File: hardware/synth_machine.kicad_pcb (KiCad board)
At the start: 2 copper layers, 234.9 x 161.9 mm, 87 parts, among them J1 USB-C (MIDI + 5V power), J10 Pot Wave (10k lin, panel moun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, J11 Pot Attack (10k lin, panel mo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, J12 Pot Decay (10k lin, panel mou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, J13 Pot Sustain (10k lin, panel m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, J14 Pot Release (10k lin, panel m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, J4 From amp screw terminals (L+ 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, J5 Speaker L (JST-PH), J6 Speaker R (JST-PH), J7 Headphones 3.5mm (CUI SJ1-351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, J8 Expansion, Q1 2N3904, SW1 KEY C4 (direct D10) - 2x Keys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, SW10 D#4 [c4 r1] - 2x Keystone 3534, SW11 F#4 [c3 r1] - 2x Keystone 3534, SW12 G#4 [c2 r1] - 2x Keystone 3534, SW13 A#4 [c1 r1] - 2x Keystone 3534, SW14 BTN1 [c0 r0] - 2x Keystone 35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, SW15 BTN2 [c0 r1] - 2x Keystone 35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, SW16 BTN3 [c1 r0] - 2x Keystone 35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, SW17 BTN4 [c2 r0] - 2x Keystone 35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, SW18 BTN5 [c3 r0] - 2x Keystone 35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, SW19 BTN6 [c4 r0] - 2x Keystone 35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, SW2 D4 [c5 r1] - 2x Keystone 3534, SW3 E4 [c5 r2] - 2x Keystone 3534, SW4 F4 [c4 r2] - 2x Keystone 3534, SW5 G4 [c3 r2] - 2x Keystone 3534, SW6 A4 [c2 r2] - 2x Keystone 3534, SW7 B4 [c1 r2] - 2x Keystone 3534, SW8 C5 [c0 r2] - 2x Keystone 3534, SW9 C#4 [c5 r0] - 2x Keystone 3534, U1 Daisy Seed, U2 TPA6138A2PWR

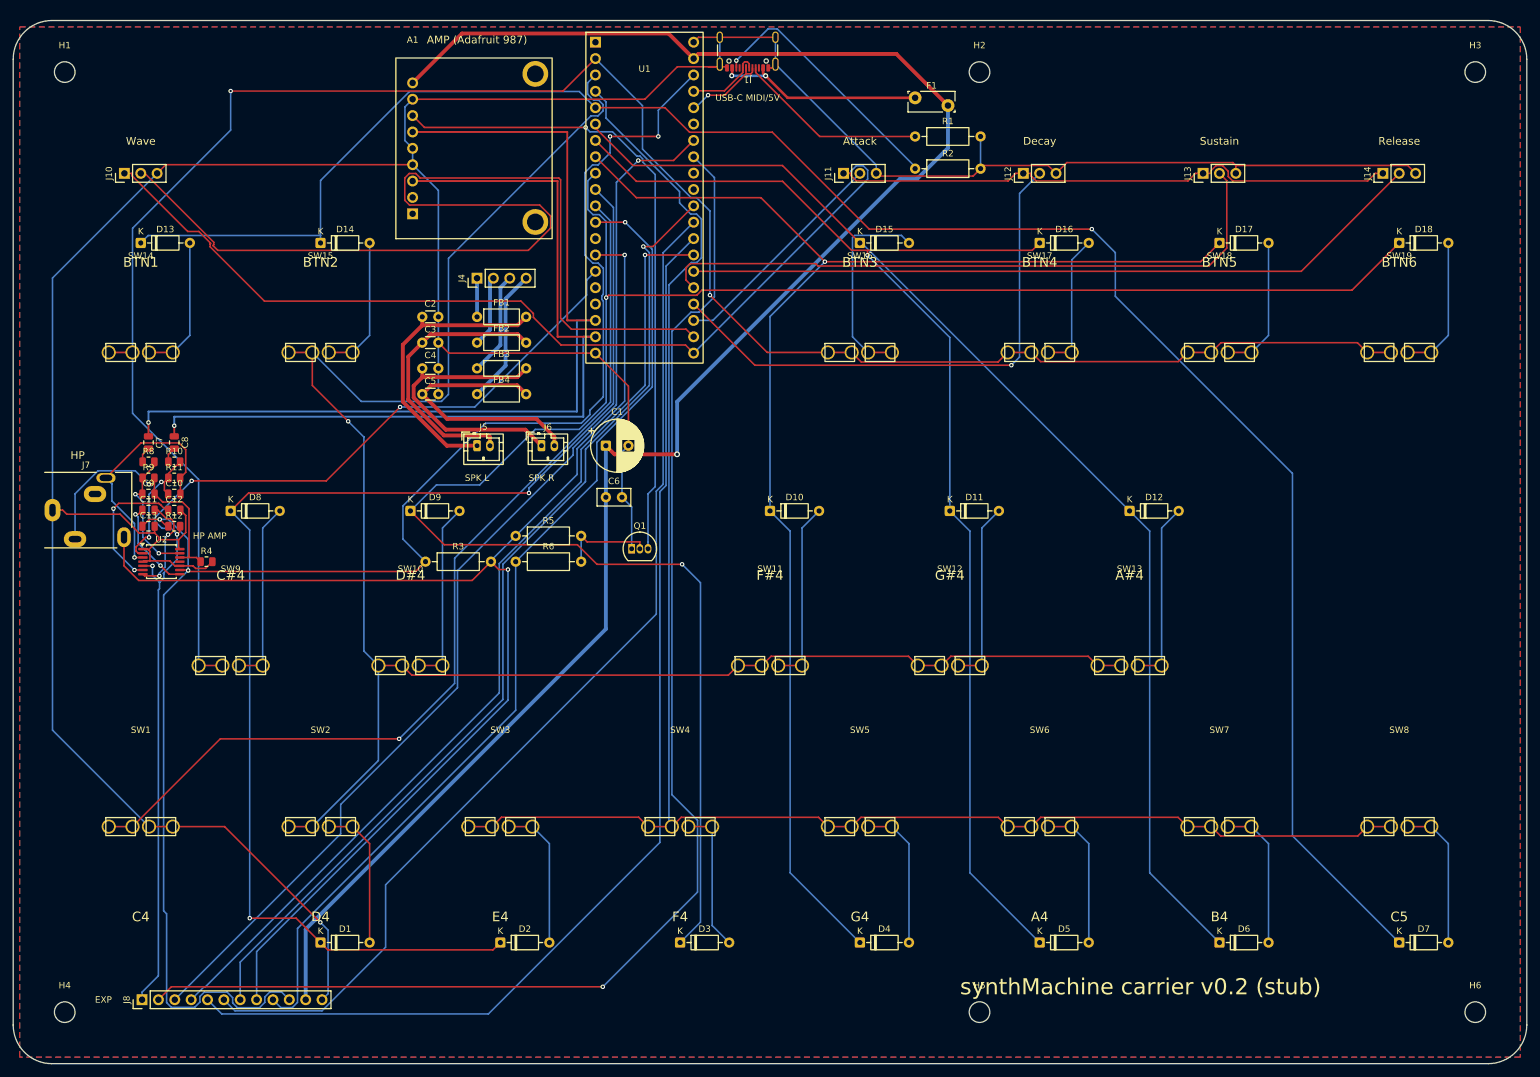
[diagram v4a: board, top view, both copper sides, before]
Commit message: Put the MAX98306 on the board and prepare for JLCPCB SMT assembly
- U3 MAX98306ETD+T (TDFN-14, thermal vias) replaces the Adafruit breakout
  header A1 and the speaker return header J4; 1u input caps, 10u + 100n
  decoupling, 100k SHDN pull-up, 100k gain resistor (9 dB) and a 3-pad
  solder jumper for 12/18 dB
- amp fan-out hand-routed: 0.2 mm stubs from the 0.4 mm pitch pads, vias,
  0.3 mm B.Cu bus to the ferrite beads; speaker nets renamed to P/N so
  KiCad/Freerouting stop treating them as differential pairs
- design rules 0.2 mm track / 0.15 mm clearance / 0.2 mm min drill
- all SMD passives are 0805 with LCSC codes; CC pull-downs and the
  headphone-detect resistors moved from axial to 0805
- fab.sh emits jlcpcb_bom.csv / jlcpcb_cpl.csv for top-side assembly
- routed: 915 segments, 61 vias, 0 unrouted, DRC clean apart from known nits

Co-Authored-By: Claude Fable 5.1 <noreply@anthropic.com>
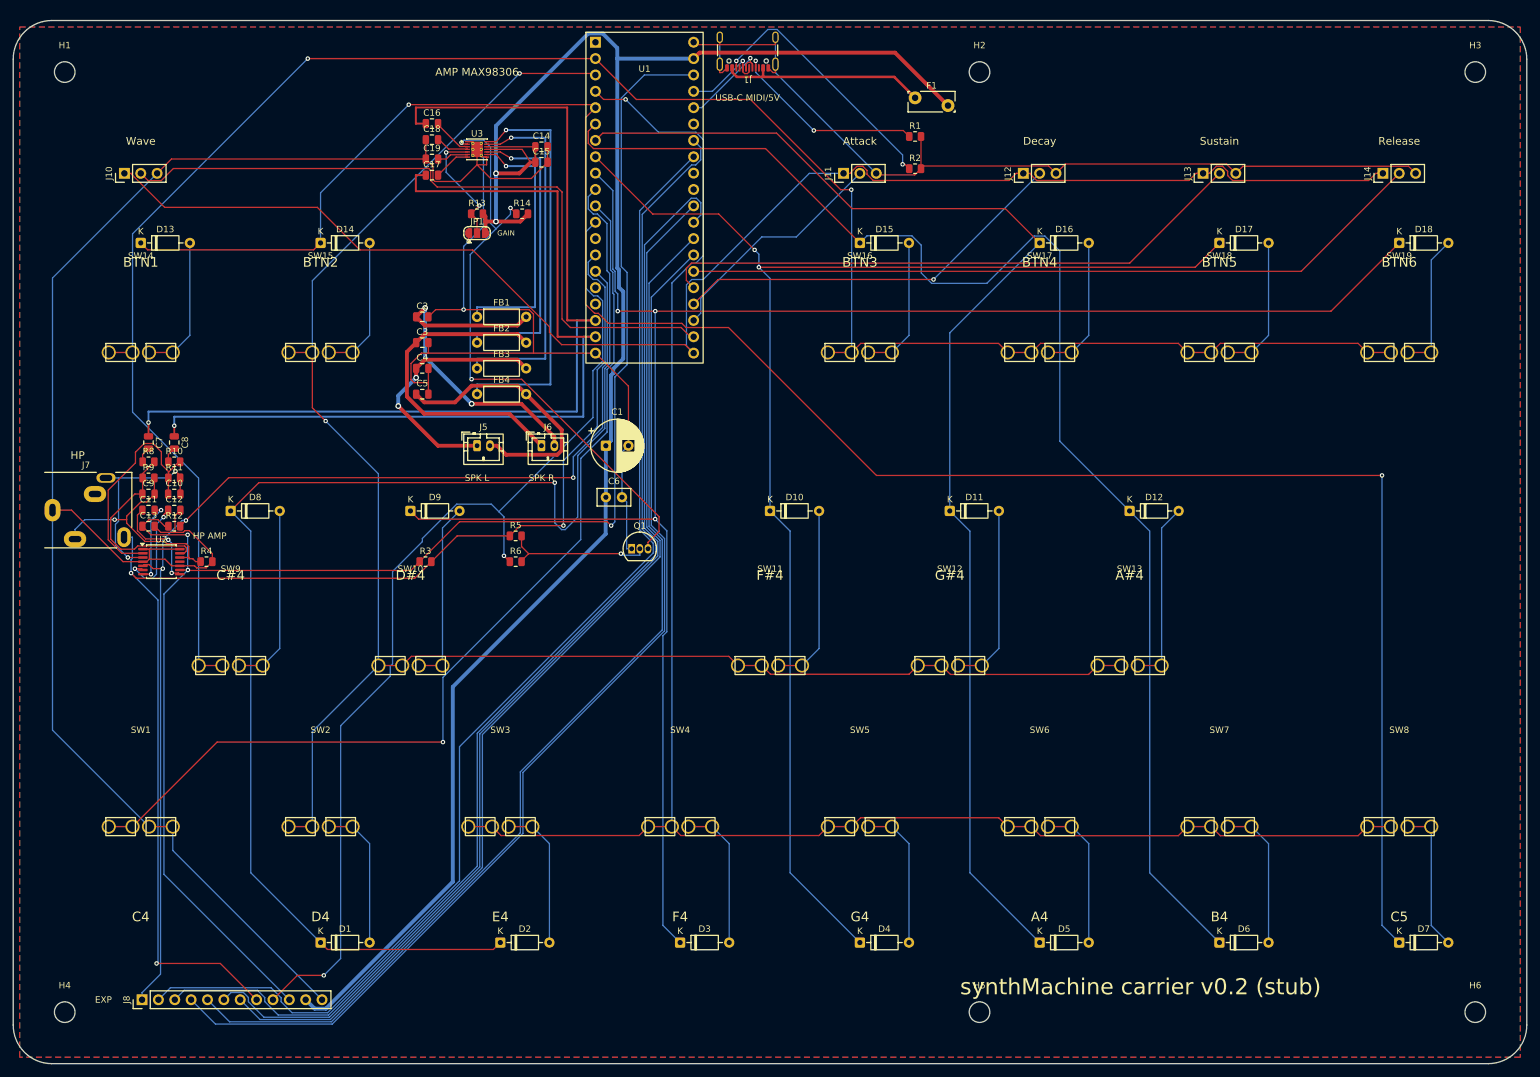
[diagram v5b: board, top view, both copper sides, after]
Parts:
- removed A1: Adafruit MAX98306 amp breakout, Adafruit_MAX98306_Breakout
- removed J4: From amp screw terminals (L+ L- R+ R-), PinHeader_1x04_P2.54mm_Vertical
- added C14: 10u, C_0805_2012Metric, F.Cu at (82.0, 19.6)
- added C15: 100n, C_0805_2012Metric, F.Cu at (82.0, 22.0)
- added C16: 1u, C_0805_2012Metric, F.Cu at (65.0, 16.0)
- added C17: 1u, C_0805_2012Metric, F.Cu at (65.0, 24.0)
- added C18: 1u, C_0805_2012Metric, F.Cu at (65.0, 18.5)
- added C19: 1u, C_0805_2012Metric, F.Cu at (65.0, 21.5)
- added JP1: GAIN: 1-2 = 18dB, open = R13, 2-3 = 12dB, SolderJumper-3_P1.3mm_Open_RoundedPad1.0x1.5mm, F.Cu at (72.0, 33.0)
- added R13: 100k, R_0805_2012Metric, F.Cu at (72.0, 30.0)
- added R14: 100k, R_0805_2012Metric, F.Cu at (79.0, 30.0)
- added U3: MAX98306ETD+T, TDFN-14-1EP_3x3mm_P0.4mm_EP1.78x2.35mm_ThermalVias, F.Cu at (72.0, 20.0)
- C13: value 2u2 -> 10u
- C2, C3, C4, C5: footprint C_Disc_D3.0mm_W1.6mm_P2.50mm -> C_0805_2012Metric
- R1, R2, R3, R5, R6: footprint R_Axial_DIN0207_L6.3mm_D2.5mm_P10.16mm_Horizontal -> R_0805_2012Metric
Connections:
- C2 pad 1: SPKF_L+ -> SPKF_RN
- C3 pad 1: SPKF_L- -> SPKF_RP
- C4 pad 1: SPKF_R+ -> SPKF_LP
- C5 pad 1: SPKF_R- -> SPKF_LN
- FB1 pad 1: SPK_L+ -> SPK_RN
- FB1 pad 2: SPKF_L+ -> SPKF_RN
- FB2 pad 1: SPK_L- -> SPK_RP
- FB2 pad 2: SPKF_L- -> SPKF_RP
- FB3 pad 1: SPK_R+ -> SPK_LP
- FB3 pad 2: SPKF_R+ -> SPKF_LP
- FB4 pad 1: SPK_R- -> SPK_LN
- FB4 pad 2: SPKF_R- -> SPKF_LN
- J5 pad 1: SPKF_L+ -> SPKF_LP
- J5 pad 2: SPKF_L- -> SPKF_LN
- J6 pad 1: SPKF_R+ -> SPKF_RP
- J6 pad 2: SPKF_R- -> SPKF_RN
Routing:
- net SPK_LN: track 0.00 -> 63.2 mm, vias 0 -> 1
- net POT_WAVE: track 167.7 -> 110.4 mm
- net SPK_LP: track 0.00 -> 55.8 mm, vias 0 -> 1
- net SPKF_RN: track 0.00 -> 54.4 mm, vias 0 -> 2
- net SPKF_RP: track 0.00 -> 51.2 mm
- net SPK_RP: track 0.00 -> 47.0 mm, vias 0 -> 1
- net SPKF_L+: track 45.4 -> 0.00 mm
- net SPKF_R+: track 44.7 -> 0.00 mm
- net SPKF_L-: track 43.4 -> 0.00 mm
- net SPKF_LN: track 0.00 -> 42.2 mm
- net SPKF_R-: track 41.9 -> 0.00 mm
- net SPK_RN: track 0.00 -> 40.8 mm, vias 0 -> 1
- net SPKF_LP: track 0.00 -> 40.0 mm, vias 0 -> 2
- net COL1: track 180.9 -> 210.7 mm
- net EXP_D26: track 211.2 -> 187.2 mm, vias 1 -> 0
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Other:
- board text added: "AMP MAX98306"
- board text added: "GAIN"
- board text removed: "AMP (Adafruit 987)"

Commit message: Carrier v0.3: compact 100x100 board, JST-XH leads for buttons and pots
- Buttons no longer plug into the board: one JST-XH 2-pin header per key
  (10 down the left edge, 9 along the bottom), pots on JST-XH 3-pin headers
  down the right edge; board shrinks to 100 x 100 mm (JLC cheap tier)
- USB-C, headphone jack and the Seed's own USB all on the top edge
- Seed3 supported (same pinout/outline as the original Seed)
- more SMT for JLC: 1N4148W SOD-123 diodes, 0805 ferrite beads, MMBT3904
  SOT-23, 0805 100n; hand-solder list is now connectors, sockets, fuse, C1
- audio pre-routes reworked for the new geometry (no crossings), amp
  fan-out kept; 808 segments, 46 vias, 0 unrouted, DRC clean apart from the
  known library nits
- README rewritten; Digi-Key list rewritten for the XH connectors

Co-Authored-By: Claude Fable 5.1 <noreply@anthropic.com>
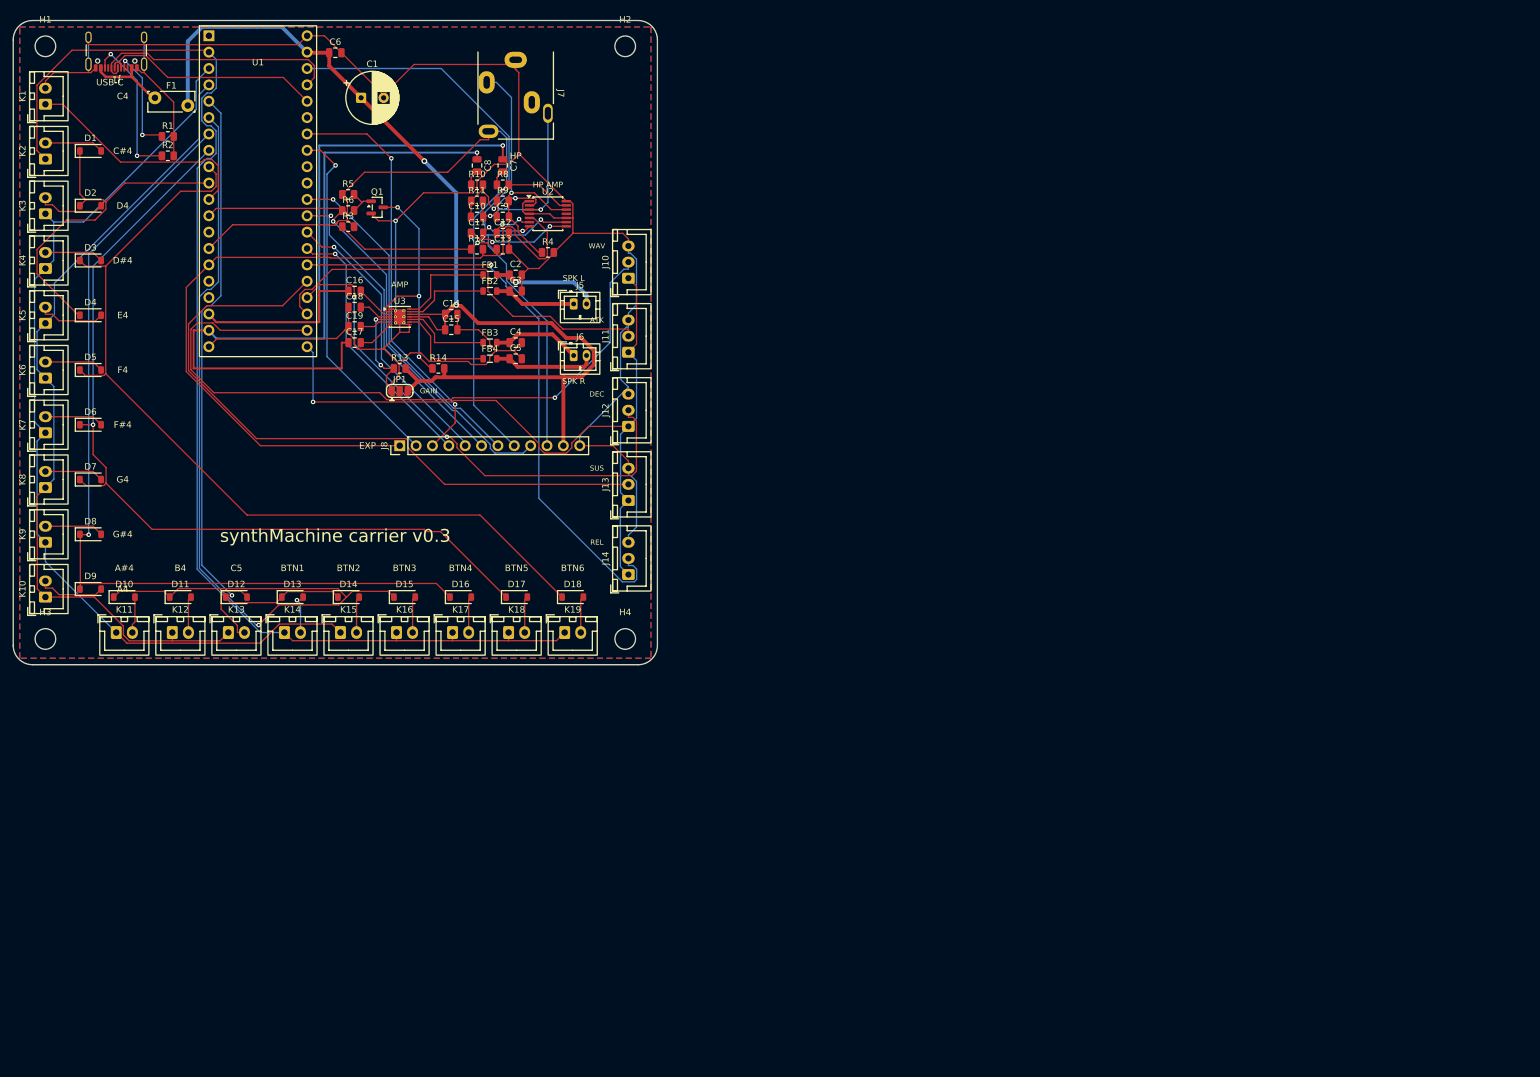
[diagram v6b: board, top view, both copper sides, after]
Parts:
- removed H5, H6: M3, MountingHole_3.2mm_M3
- removed SW1: KEY C4 (direct D10) - 2x Keystone 3534, ArcadeButton_24mm_Keystone3534
- removed SW10: D#4 [c4 r1] - 2x Keystone 3534, ArcadeButton_24mm_Keystone3534
- removed SW11: F#4 [c3 r1] - 2x Keystone 3534, ArcadeButton_24mm_Keystone3534
- removed SW12: G#4 [c2 r1] - 2x Keystone 3534, ArcadeButton_24mm_Keystone3534
- removed SW13: A#4 [c1 r1] - 2x Keystone 3534, ArcadeButton_24mm_Keystone3534
- removed SW14: BTN1 [c0 r0] - 2x Keystone 3534, ArcadeButton_24mm_Keystone3534
- removed SW15: BTN2 [c0 r1] - 2x Keystone 3534, ArcadeButton_24mm_Keystone3534
- removed SW16: BTN3 [c1 r0] - 2x Keystone 3534, ArcadeButton_24mm_Keystone3534
- removed SW17: BTN4 [c2 r0] - 2x Keystone 3534, ArcadeButton_24mm_Keystone3534
- removed SW18: BTN5 [c3 r0] - 2x Keystone 3534, ArcadeButton_24mm_Keystone3534
- removed SW19: BTN6 [c4 r0] - 2x Keystone 3534, ArcadeButton_24mm_Keystone3534
- removed SW2: D4 [c5 r1] - 2x Keystone 3534, ArcadeButton_24mm_Keystone3534
- removed SW3: E4 [c5 r2] - 2x Keystone 3534, ArcadeButton_24mm_Keystone3534
- removed SW4: F4 [c4 r2] - 2x Keystone 3534, ArcadeButton_24mm_Keystone3534
- removed SW5: G4 [c3 r2] - 2x Keystone 3534, ArcadeButton_24mm_Keystone3534
- removed SW6: A4 [c2 r2] - 2x Keystone 3534, ArcadeButton_24mm_Keystone3534
- removed SW7: B4 [c1 r2] - 2x Keystone 3534, ArcadeButton_24mm_Keystone3534
- removed SW8: C5 [c0 r2] - 2x Keystone 3534, ArcadeButton_24mm_Keystone3534
- removed SW9: C#4 [c5 r0] - 2x Keystone 3534, ArcadeButton_24mm_Keystone3534
- added K1: KEY C4 (direct D10) JST-XH, JST_XH_B2B-XH-A_1x02_P2.50mm_Vertical, F.Cu at (5.00, 13.0)
- added K10: A4 [c2 r2] JST-XH, JST_XH_B2B-XH-A_1x02_P2.50mm_Vertical, F.Cu at (5.00, 89.5)
- added K11: A#4 [c1 r1] JST-XH, JST_XH_B2B-XH-A_1x02_P2.50mm_Vertical, F.Cu at (16.0, 95.0)
- added K12: B4 [c1 r2] JST-XH, JST_XH_B2B-XH-A_1x02_P2.50mm_Vertical, F.Cu at (24.7, 95.0)
- added K13: C5 [c0 r2] JST-XH, JST_XH_B2B-XH-A_1x02_P2.50mm_Vertical, F.Cu at (33.4, 95.0)
- added K14: BTN1 [c0 r0] JST-XH, JST_XH_B2B-XH-A_1x02_P2.50mm_Vertical, F.Cu at (42.1, 95.0)
- added K15: BTN2 [c0 r1] JST-XH, JST_XH_B2B-XH-A_1x02_P2.50mm_Vertical, F.Cu at (50.8, 95.0)
- added K16: BTN3 [c1 r0] JST-XH, JST_XH_B2B-XH-A_1x02_P2.50mm_Vertical, F.Cu at (59.5, 95.0)
- added K17: BTN4 [c2 r0] JST-XH, JST_XH_B2B-XH-A_1x02_P2.50mm_Vertical, F.Cu at (68.2, 95.0)
- added K18: BTN5 [c3 r0] JST-XH, JST_XH_B2B-XH-A_1x02_P2.50mm_Vertical, F.Cu at (76.9, 95.0)
- added K19: BTN6 [c4 r0] JST-XH, JST_XH_B2B-XH-A_1x02_P2.50mm_Vertical, F.Cu at (85.6, 95.0)
- added K2: C#4 [c5 r0] JST-XH, JST_XH_B2B-XH-A_1x02_P2.50mm_Vertical, F.Cu at (5.00, 21.5)
- added K3: D4 [c5 r1] JST-XH, JST_XH_B2B-XH-A_1x02_P2.50mm_Vertical, F.Cu at (5.00, 30.0)
- added K4: D#4 [c4 r1] JST-XH, JST_XH_B2B-XH-A_1x02_P2.50mm_Vertical, F.Cu at (5.00, 38.5)
- added K5: E4 [c5 r2] JST-XH, JST_XH_B2B-XH-A_1x02_P2.50mm_Vertical, F.Cu at (5.00, 47.0)
- added K6: F4 [c4 r2] JST-XH, JST_XH_B2B-XH-A_1x02_P2.50mm_Vertical, F.Cu at (5.00, 55.5)
- added K7: F#4 [c3 r1] JST-XH, JST_XH_B2B-XH-A_1x02_P2.50mm_Vertical, F.Cu at (5.00, 64.0)
- added K8: G4 [c3 r2] JST-XH, JST_XH_B2B-XH-A_1x02_P2.50mm_Vertical, F.Cu at (5.00, 72.5)
- added K9: G#4 [c2 r1] JST-XH, JST_XH_B2B-XH-A_1x02_P2.50mm_Vertical, F.Cu at (5.00, 81.0)
- C6: footprint C_Disc_D5.0mm_W2.5mm_P2.50mm -> C_0805_2012Metric
- D1, D10, D11, D12, D13, D14, D15, D16, D17, D18, D2, D3, D4, D5, D6, D7, D8, D9: value 1N4148 -> 1N4148W; footprint D_DO-35_SOD27_P7.62mm_Horizontal -> D_SOD-123
- F1: value 2A hold PTC (MF-R200) -> MF-R250 2.5A PTC
- FB1, FB2, FB3, FB4: value 600R@100MHz -> 100R@100MHz 0805; footprint L_Axial_L5.3mm_D2.2mm_P7.62mm_Horizontal_Vishay_IM-1 -> L_0805_2012Metric
- J10: value Pot Wave (10k lin, panel mount) -> Pot WAV (10k lin, panel) JST-XH; footprint PinHeader_1x03_P2.54mm_Vertical -> JST_XH_B3B-XH-A_1x03_P2.50mm_Vertical
- J11: value Pot Attack (10k lin, panel mount) -> Pot ATK (10k lin, panel) JST-XH; footprint PinHeader_1x03_P2.54mm_Vertical -> JST_XH_B3B-XH-A_1x03_P2.50mm_Vertical
- J12: value Pot Decay (10k lin, panel mount) -> Pot DEC (10k lin, panel) JST-XH; footprint PinHeader_1x03_P2.54mm_Vertical -> JST_XH_B3B-XH-A_1x03_P2.50mm_Vertical
- J13: value Pot Sustain (10k lin, panel mount) -> Pot SUS (10k lin, panel) JST-XH; footprint PinHeader_1x03_P2.54mm_Vertical -> JST_XH_B3B-XH-A_1x03_P2.50mm_Vertical
- J14: value Pot Release (10k lin, panel mount) -> Pot REL (10k lin, panel) JST-XH; footprint PinHeader_1x03_P2.54mm_Vertical -> JST_XH_B3B-XH-A_1x03_P2.50mm_Vertical
- Q1: value 2N3904 -> MMBT3904; footprint TO-92_Inline -> SOT-23
- U1: value Daisy Seed -> Daisy Seed / Seed3
- moved H3 238.8 mm to (5.00, 96.0)
- moved D7 215.5 mm to (12.0, 71.2)
- moved D6 192.8 mm to (12.0, 62.8)
- moved D5 172.1 mm to (12.0, 54.2)
- moved D4 154.1 mm to (12.0, 45.8)
- moved D3 139.9 mm to (12.0, 37.2)
- moved D18 139.6 mm to (86.8, 89.5)
- moved D12 139.3 mm to (34.6, 89.5)
- moved J14 132.6 mm to (95.5, 86.0)
- moved D2 130.9 mm to (12.0, 28.8)
- moved D1 128.0 mm to (12.0, 20.2)
- moved D17 122.2 mm to (78.2, 89.5)
- moved D11 120.2 mm to (25.9, 89.5)
- moved F1 118.0 mm to (22.0, 12.0)
- moved R2 116.0 mm to (24.0, 21.0)
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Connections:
- C2 pad 1: SPKF_RN -> SPKF_LN
- C3 pad 1: SPKF_RP -> SPKF_LP
- C4 pad 1: SPKF_LP -> SPKF_RP
- C5 pad 1: SPKF_LN -> SPKF_RN
- D1 pad 2: KD4_D -> KCs4_D
- D10 pad 1: COL3 -> COL1
- D10 pad 2: KFs4_D -> KAs4_D
- D11 pad 1: COL2 -> COL1
- D11 pad 2: KGs4_D -> KB4_D
- D12 pad 1: COL1 -> COL0
- D12 pad 2: KAs4_D -> KC5_D
- D2 pad 2: KE4_D -> KD4_D
- D3 pad 2: KF4_D -> KDs4_D
- D4 pad 1: COL3 -> COL5
- D4 pad 2: KG4_D -> KE4_D
- D5 pad 1: COL2 -> COL4
- D5 pad 2: KA4_D -> KF4_D
- D6 pad 1: COL1 -> COL3
- D6 pad 2: KB4_D -> KFs4_D
- D7 pad 1: COL0 -> COL3
- D7 pad 2: KC5_D -> KG4_D
- D8 pad 1: COL5 -> COL2
- D8 pad 2: KCs4_D -> KGs4_D
- D9 pad 1: COL4 -> COL2
- D9 pad 2: KDs4_D -> KA4_D
- FB1 pad 1: SPK_RN -> SPK_LN
- FB1 pad 2: SPKF_RN -> SPKF_LN
- FB2 pad 1: SPK_RP -> SPK_LP
- FB2 pad 2: SPKF_RP -> SPKF_LP
- FB3 pad 1: SPK_LP -> SPK_RP
- FB3 pad 2: SPKF_LP -> SPKF_RP
- FB4 pad 1: SPK_LN -> SPK_RN
- FB4 pad 2: SPKF_LN -> SPKF_RN
- Q1 pad 1: GND -> Q1_B
- Q1 pad 2: Q1_B -> GND
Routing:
- net COL0: track 324.5 -> 100.9 mm, vias 2 -> 1
- net GND: track 559.8 -> 378.0 mm, vias 2 -> 1
- net COL5: track 219.9 -> 57.2 mm, vias 1 -> 0
- net ROW2: track 277.9 -> 127.1 mm, vias 1 -> 0
- net COL4: track 287.2 -> 136.5 mm, vias 3 -> 0
- net ROW0: track 326.2 -> 192.0 mm, vias 2 -> 0
- net +5V: track 303.0 -> 170.5 mm
- net EXP_D26: track 187.2 -> 55.2 mm, vias 0 -> 1
- net ROW1: track 276.8 -> 146.9 mm, vias 2 -> 0
- net EXP_A7: track 176.2 -> 49.3 mm, vias 0 -> 1
- net EXP_A5: track 167.8 -> 41.8 mm, vias 0 -> 1
- net EXP_D27: track 188.7 -> 64.8 mm, vias 0 -> 2
- net EXP_A6: track 167.2 -> 44.4 mm, vias 0 -> 1
- net +3.3VA: track 232.4 -> 114.1 mm, vias 0 -> 1
- net KEY_C4: track 152.7 -> 37.0 mm, vias 1 -> 0
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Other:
- board size 234.9 x 161.9 mm -> 100 x 100 mm
- board text added: "AMP"
- board text added: "ATK"
- board text added: "DEC"
- board text added: "REL"
- board text added: "SUS"
- board text added: "USB-C"
- board text added: "WAV"
- board text added: "synthMachine carrier v0.3"
- board text removed: "AMP MAX98306"
- board text removed: "Attack"
- board text removed: "Decay"
- board text removed: "Release"
- board text removed: "Sustain"
- board text removed: "USB-C MIDI/5V"
- board text removed: "Wave"
- board text removed: "synthMachine carrier v0.2 (stub)"
